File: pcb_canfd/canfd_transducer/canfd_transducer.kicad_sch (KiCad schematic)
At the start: 7 parts, among them J1 Conn_01x13_Female, J2 Conn_01x03_Female, U1 MCP2517FD-xSL

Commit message: finished first version of board, needs revision
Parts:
- added H1, H2, H3, H4: MountingHole, MountingHole:MountingHole_3.2mm_M3_DIN965_Pad_TopOnly, symbol Mechanical:MountingHole
- J1: footprint Connector_PinHeader_2.54mm:PinHeader_1x13_P2.54mm_Vertical -> Connector_PinSocket_2.54mm:PinSocket_1x13_P2.54mm_Vertical
- renumbered 11 to U2
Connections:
- net +3.3V: now also J1.3 (Pin_3); no longer J1.2 (Pin_2)
- net CANH: now also J2.1 (Pin_1); no longer J2.2 (Pin_2)
- net CANL: now also J2.2 (Pin_2); no longer J2.3 (Pin_3)
- net CLKO: now also J1.13 (Pin_13); no longer J1.8 (Pin_8)
- net GND: now also J1.2 (Pin_2), J2.3 (Pin_3); no longer J1.3 (Pin_3)
- net OSC2: now also J1.11 (Pin_11); no longer J1.9 (Pin_9)
- net SDI: now also J1.6 (Pin_6); no longer J1.4 (Pin_4)
- net nCS: now also J1.4 (Pin_4); no longer J1.6 (Pin_6)
- net ~{INT0}: now also J1.8 (Pin_8); no longer J1.12 (Pin_12)
- net ~{INT1}: now also J1.9 (Pin_9); no longer J1.11 (Pin_11)
- net ~{INT}: now also J1.12 (Pin_12); no longer J1.13 (Pin_13)

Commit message: small changes
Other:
- company: (none) -> Group 3 - ME410, EPFL
- title: (none) -> SPI to can FD transducer
- moved on the sheet: H1, H2, H3, H4
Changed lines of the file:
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@@
 (kicad_sch (version 20211123) (generator eeschema)
   (paper "A4")
+  (title_block
+    (title "SPI to can FD transducer")
+    (date "2023-10-23")
+    (company "Group 3 - ME410, EPFL")
+  )
   (junction (at 81.28 67.31) (diameter 0) (color 0 0 0 0)
   )
@@
     (pin "2")
   )
-  (symbol (lib_id "Mechanical:MountingHole") (at 252.73 124.46 0) (unit 1)
-    (in_bom yes) (on_board yes) (fields_autoplaced)
-    (property "Reference" "H3" (id 0) (at 255.27 123.1899 0)
-      (effects (font (size 1.27 1.27)) (justify left))
-    )
-    (property "Value" "MountingHole" (id 1) (at 255.27 125.7299 0)
-      (effects (font (size 1.27 1.27)) (justify left))
-    )
-    (property "Footprint" "MountingHole:MountingHole_3.2mm_M3_DIN965_Pad_TopOnly" (id 2) (at 252.73 124.46 0)
-      (effects (font (size 1.27 1.27)) hide)
-    )
-    (property "Datasheet" "~" (id 3) (at 252.73 124.46 0)
+  (symbol (lib_id "Mechanical:MountingHole") (at 234.95 57.15 0) (unit 1)
+    (in_bom yes) (on_board yes) (fields_autoplaced)
+    (property "Reference" "H3" (id 0) (at 237.49 55.8799 0)
+      (effects (font (size 1.27 1.27)) (justify left))
+    )
+    (property "Value" "MountingHole" (id 1) (at 237.49 58.4199 0)
+      (effects (font (size 1.27 1.27)) (justify left))
+    )
+    (property "Footprint" "MountingHole:MountingHole_3.2mm_M3_DIN965_Pad_TopOnly" (id 2) (at 234.95 57.15 0)
+      (effects (font (size 1.27 1.27)) hide)
+    )
+    (property "Datasheet" "~" (id 3) (at 234.95 57.15 0)
       (effects (font (size 1.27 1.27)) hide)
     )
@@
     (pin "8")
   )
-  (symbol (lib_id "Mechanical:MountingHole") (at 252.73 130.81 0) (unit 1)
-    (in_bom yes) (on_board yes) (fields_autoplaced)
-    (property "Reference" "H4" (id 0) (at 255.27 129.5399 0)
-      (effects (font (size 1.27 1.27)) (justify left))
-    )
-    (property "Value" "MountingHole" (id 1) (at 255.27 132.0799 0)
-      (effects (font (size 1.27 1.27)) (justify left))
-    )
-    (property "Footprint" "MountingHole:MountingHole_3.2mm_M3_DIN965_Pad_TopOnly" (id 2) (at 252.73 130.81 0)
-      (effects (font (size 1.27 1.27)) hide)
-    )
-    (property "Datasheet" "~" (id 3) (at 252.73 130.81 0)
+  (symbol (lib_id "Mechanical:MountingHole") (at 234.95 63.5 0) (unit 1)
+    (in_bom yes) (on_board yes) (fields_autoplaced)
+    (property "Reference" "H4" (id 0) (at 237.49 62.2299 0)
+      (effects (font (size 1.27 1.27)) (justify left))
+    )
+    (property "Value" "MountingHole" (id 1) (at 237.49 64.7699 0)
+      (effects (font (size 1.27 1.27)) (justify left))
+    )
+    (property "Footprint" "MountingHole:MountingHole_3.2mm_M3_DIN965_Pad_TopOnly" (id 2) (at 234.95 63.5 0)
+      (effects (font (size 1.27 1.27)) hide)
+    )
+    (property "Datasheet" "~" (id 3) (at 234.95 63.5 0)
       (effects (font (size 1.27 1.27)) hide)
     )
@@
     (pin "1")
   )
-  (symbol (lib_id "Mechanical:MountingHole") (at 252.73 118.11 0) (unit 1)
-    (in_bom yes) (on_board yes) (fields_autoplaced)
-    (property "Reference" "H2" (id 0) (at 255.27 116.8399 0)
-      (effects (font (size 1.27 1.27)) (justify left))
-    )
-    (property "Value" "MountingHole" (id 1) (at 255.27 119.3799 0)
-      (effects (font (size 1.27 1.27)) (justify left))
-    )
-    (property "Footprint" "MountingHole:MountingHole_3.2mm_M3_DIN965_Pad_TopOnly" (id 2) (at 252.73 118.11 0)
-      (effects (font (size 1.27 1.27)) hide)
-    )
-    (property "Datasheet" "~" (id 3) (at 252.73 118.11 0)
+  (symbol (lib_id "Mechanical:MountingHole") (at 234.95 50.8 0) (unit 1)
+    (in_bom yes) (on_board yes) (fields_autoplaced)
+    (property "Reference" "H2" (id 0) (at 237.49 49.5299 0)
+      (effects (font (size 1.27 1.27)) (justify left))
+    )
+    (property "Value" "MountingHole" (id 1) (at 237.49 52.0699 0)
+      (effects (font (size 1.27 1.27)) (justify left))
+    )
+    (property "Footprint" "MountingHole:MountingHole_3.2mm_M3_DIN965_Pad_TopOnly" (id 2) (at 234.95 50.8 0)
+      (effects (font (size 1.27 1.27)) hide)
+    )
+    (property "Datasheet" "~" (id 3) (at 234.95 50.8 0)
       (effects (font (size 1.27 1.27)) hide)
     )
@@
     (pin "1")
   )
-  (symbol (lib_id "Mechanical:MountingHole") (at 252.73 111.76 0) (unit 1)
-    (in_bom yes) (on_board yes) (fields_autoplaced)
-    (property "Reference" "H1" (id 0) (at 255.27 110.4899 0)
-      (effects (font (size 1.27 1.27)) (justify left))
-    )
-    (property "Value" "MountingHole" (id 1) (at 255.27 113.0299 0)
-      (effects (font (size 1.27 1.27)) (justify left))
-    )
-    (property "Footprint" "MountingHole:MountingHole_3.2mm_M3_DIN965_Pad_TopOnly" (id 2) (at 252.73 111.76 0)
-      (effects (font (size 1.27 1.27)) hide)
-    )
-    (property "Datasheet" "~" (id 3) (at 252.73 111.76 0)
-      (effects (font (size 1.27 1.27)) hide)
-    )
+  (symbol (lib_id "Mechanical:MountingHole") (at 234.95 44.45 0) (unit 1)
+    (in_bom yes) (on_board yes) (fields_autoplaced)
+    (property "Reference" "H1" (id 0) (at 237.49 43.1799 0)
+      (effects (font (size 1.27 1.27)) (justify left))
+    )
+    (property "Value" "MountingHole" (id 1) (at 237.49 45.7199 0)
+      (effects (font (size 1.27 1.27)) (justify left))
+    )
+    (property "Footprint" "MountingHole:MountingHole_3.2mm_M3_DIN965_Pad_TopOnly" (id 2) (at 234.95 44.45 0)
+      (effects (font (size 1.27 1.27)) hide)
+    )
+    (property "Datasheet" "~" (id 3) (at 234.95 44.45 0)
+      (effects (font (size 1.27 1.27)) hide)
+    )

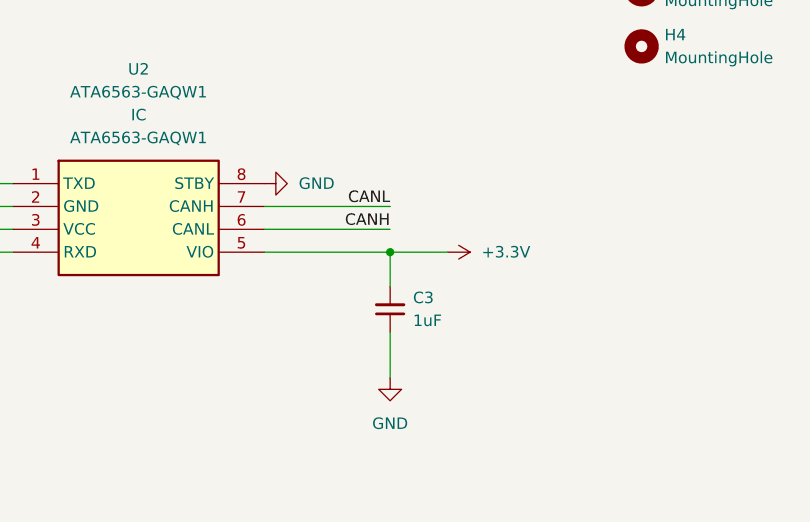
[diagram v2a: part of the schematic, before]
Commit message: added resistor for can bus
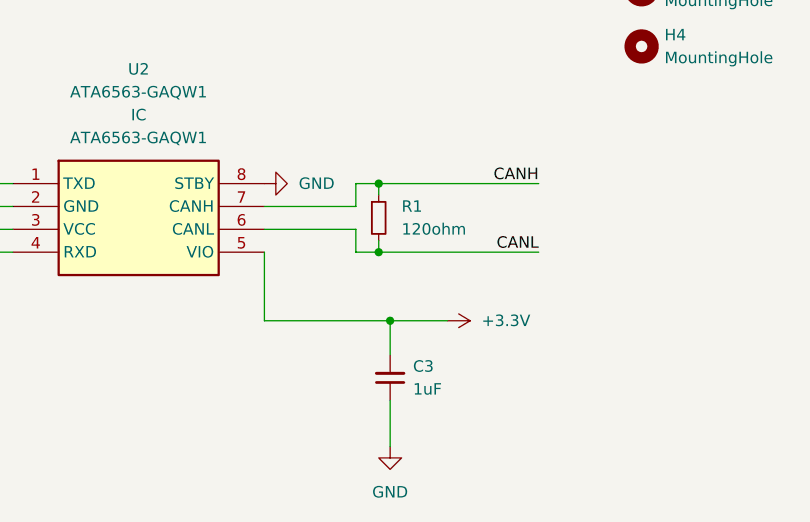
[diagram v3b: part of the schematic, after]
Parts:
- added R1: 120ohm, Resistor_SMD:R_0805_2012Metric, symbol Device:R_Small
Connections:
- net CANH: now also U2.7 (CANH), R1.1; no longer U2.6 (CANL)
- net CANL: now also U2.6 (CANL), R1.2; no longer U2.7 (CANH)
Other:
- moved on the sheet: C3
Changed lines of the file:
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@@
     (company "Group 3 - ME410, EPFL")
   )
+  (junction (at 205.74 78.74) (diameter 0) (color 0 0 0 0)
+  )
+  (junction (at 207.01 93.98) (diameter 0) (color 0 0 0 0)
+  )
+  (junction (at 205.74 86.36) (diameter 0) (color 0 0 0 0)
+  )
   (junction (at 81.28 67.31) (diameter 0) (color 0 0 0 0)
   )
   (junction (at 144.78 83.82) (diameter 0) (color 0 0 0 0)
   )
-  (junction (at 207.01 86.36) (diameter 0) (color 0 0 0 0)
-  )
-  (wire (pts (xy 207.01 100.33) (xy 207.01 95.25))
+  (wire (pts (xy 207.01 107.95) (xy 207.01 102.87))
+    (stroke (width 0) (type default) (color 0 0 0 0))
+  )
+  (wire (pts (xy 205.74 78.74) (xy 223.52 78.74))
     (stroke (width 0) (type default) (color 0 0 0 0))
   )
@@
     (stroke (width 0) (type default) (color 0 0 0 0))
   )
+  (wire (pts (xy 203.2 83.82) (xy 203.2 86.36))
+    (stroke (width 0) (type default) (color 0 0 0 0))
+  )
   (wire (pts (xy 142.24 83.82) (xy 144.78 83.82))
     (stroke (width 0) (type default) (color 0 0 0 0))
@@
     (stroke (width 0) (type default) (color 0 0 0 0))
   )
+  (wire (pts (xy 205.74 86.36) (xy 223.52 86.36))
+    (stroke (width 0) (type default) (color 0 0 0 0))
+  )
+  (wire (pts (xy 203.2 86.36) (xy 205.74 86.36))
+    (stroke (width 0) (type default) (color 0 0 0 0))
+  )
   (wire (pts (xy 179.07 35.56) (xy 165.1 35.56))
     (stroke (width 0) (type default) (color 0 0 0 0))
@@
     (stroke (width 0) (type default) (color 0 0 0 0))
   )
-  (wire (pts (xy 193.04 86.36) (xy 207.01 86.36))
-    (stroke (width 0) (type default) (color 0 0 0 0))
-  )
-  (wire (pts (xy 207.01 86.36) (xy 207.01 90.17))
+  (wire (pts (xy 207.01 93.98) (xy 207.01 97.79))
     (stroke (width 0) (type default) (color 0 0 0 0))
   )
@@
     (stroke (width 0) (type default) (color 0 0 0 0))
   )
+  (wire (pts (xy 193.04 93.98) (xy 207.01 93.98))
+    (stroke (width 0) (type default) (color 0 0 0 0))
+  )
   (wire (pts (xy 66.04 67.31) (xy 71.12 67.31))
     (stroke (width 0) (type default) (color 0 0 0 0))
   )
+  (wire (pts (xy 205.74 86.36) (xy 205.74 85.09))
+    (stroke (width 0) (type default) (color 0 0 0 0))
+  )
   (wire (pts (xy 144.78 97.79) (xy 144.78 92.71))
     (stroke (width 0) (type default) (color 0 0 0 0))
   )
-  (wire (pts (xy 193.04 81.28) (xy 207.01 81.28))
+  (wire (pts (xy 203.2 81.28) (xy 203.2 78.74))
     (stroke (width 0) (type default) (color 0 0 0 0))
   )
@@
     (stroke (width 0) (type default) (color 0 0 0 0))
   )
+  (wire (pts (xy 205.74 78.74) (xy 205.74 80.01))
+    (stroke (width 0) (type default) (color 0 0 0 0))
+  )
   (wire (pts (xy 179.07 38.1) (xy 165.1 38.1))
     (stroke (width 0) (type default) (color 0 0 0 0))
   )
+  (wire (pts (xy 203.2 78.74) (xy 205.74 78.74))
+    (stroke (width 0) (type default) (color 0 0 0 0))
+  )
   (wire (pts (xy 160.02 81.28) (xy 165.1 81.28))
     (stroke (width 0) (type default) (color 0 0 0 0))
@@
     (stroke (width 0) (type default) (color 0 0 0 0))
   )
+  (wire (pts (xy 193.04 83.82) (xy 203.2 83.82))
+    (stroke (width 0) (type default) (color 0 0 0 0))
+  )
+  (wire (pts (xy 193.04 81.28) (xy 203.2 81.28))
+    (stroke (width 0) (type default) (color 0 0 0 0))
+  )
   (wire (pts (xy 96.52 78.74) (xy 109.22 78.74))
     (stroke (width 0) (type default) (color 0 0 0 0))
@@
     (stroke (width 0) (type default) (color 0 0 0 0))
   )
-  (wire (pts (xy 193.04 83.82) (xy 207.01 83.82))
-    (stroke (width 0) (type default) (color 0 0 0 0))
-  )
   (wire (pts (xy 110.49 29.21) (xy 123.19 29.21))
     (stroke (width 0) (type default) (color 0 0 0 0))
   )
-  (wire (pts (xy 207.01 86.36) (xy 213.36 86.36))
+  (wire (pts (xy 207.01 93.98) (xy 213.36 93.98))
+    (stroke (width 0) (type default) (color 0 0 0 0))
+  )
+  (wire (pts (xy 193.04 86.36) (xy 193.04 93.98))
     (stroke (width 0) (type default) (color 0 0 0 0))
   )
@@
     (effects (font (size 1.27 1.27)) (justify left bottom))
   )
-  (label "CANH" (at 207.01 83.82 180)
-    (effects (font (size 1.27 1.27)) (justify right bottom))
-  )
   (label "CLKO" (at 109.22 83.82 180)
     (effects (font (size 1.27 1.27)) (justify right bottom))
@@
     (effects (font (size 1.27 1.27)) (justify left bottom))
   )
+  (label "CANL" (at 223.52 86.36 180)
+    (effects (font (size 1.27 1.27)) (justify right bottom))
+  )
   (label "CAN_RX" (at 153.67 86.36 0)
     (effects (font (size 1.27 1.27)) (justify left bottom))
@@
   (label "OSC2" (at 52.07 91.44 0)
     (effects (font (size 1.27 1.27)) (justify left bottom))
+  )
+  (label "CANH" (at 223.52 78.74 180)
+    (effects (font (size 1.27 1.27)) (justify right bottom))
   )
   (label "SCK" (at 52.07 86.36 0)
@@
     (effects (font (size 1.27 1.27)) (justify left bottom))
   )
-  (label "CANL" (at 207.01 81.28 180)
-    (effects (font (size 1.27 1.27)) (justify right bottom))
-  )
   (label "CANH" (at 165.1 33.02 0)
     (effects (font (size 1.27 1.27)) (justify left bottom))
@@
   (symbol (lib_id "power:GND") (at 165.1 38.1 270) (unit 1)
     (in_bom yes) (on_board yes)
-    (property "Reference" "#PWR?" (id 0) (at 158.75 38.1 0)
+    (property "Reference" "#PWR0113" (id 0) (at 158.75 38.1 0)
       (effects (font (size 1.27 1.27)) hide)
     )
@@
     (pin "1")
   )
-  (symbol (lib_id "Device:C_Small") (at 207.01 92.71 180) (unit 1)
-    (in_bom yes) (on_board yes) (fields_autoplaced)
-    (property "Reference" "C3" (id 0) (at 209.55 91.4335 0)
+  (symbol (lib_id "Device:C_Small") (at 207.01 100.33 180) (unit 1)
+    (in_bom yes) (on_board yes) (fields_autoplaced)
+    (property "Reference" "C3" (id 0) (at 209.55 99.0535 0)
       (effects (font (size 1.27 1.27)) (justify right))
     )
-    (property "Value" "1uF" (id 1) (at 209.55 93.9735 0)
+    (property "Value" "1uF" (id 1) (at 209.55 101.5935 0)
       (effects (font (size 1.27 1.27)) (justify right))
     )
-    (property "Footprint" "Capacitor_SMD:C_0603_1608Metric" (id 2) (at 207.01 92.71 0)
-      (effects (font (size 1.27 1.27)) hide)
-    )
-    (property "Datasheet" "~" (id 3) (at 207.01 92.71 0)
+    (property "Footprint" "Capacitor_SMD:C_0603_1608Metric" (id 2) (at 207.01 100.33 0)
+      (effects (font (size 1.27 1.27)) hide)
+    )
+    (property "Datasheet" "~" (id 3) (at 207.01 100.33 0)
       (effects (font (size 1.27 1.27)) hide)
     )
@@
     (pin "7")
     (pin "8")
+  )
+  (symbol (lib_id "Device:R_Small") (at 205.74 82.55 0) (unit 1)
+    (in_bom yes) (on_board yes)
+    (property "Reference" "R1" (id 0) (at 208.28 81.2799 0)
+      (effects (font (size 1.27 1.27)) (justify left))
+    )
+    (property "Value" "120ohm" (id 1) (at 208.28 83.82 0)
+      (effects (font (size 1.27 1.27)) (justify left))
+    )
+    (property "Footprint" "Resistor_SMD:R_0805_2012Metric" (id 2) (at 205.74 82.55 0)
+      (effects (font (size 1.27 1.27)) hide)
+    )
+    (property "Datasheet" "~" (id 3) (at 205.74 82.55 0)
+      (effects (font (size 1.27 1.27)) hide)
+    )
+    (pin "1")
+    (pin "2")
   )
   (symbol (lib_id "Mechanical:MountingHole") (at 234.95 63.5 0) (unit 1)
@@
     (pin "1")
   )
-  (symbol (lib_id "power:GND") (at 207.01 100.33 0) (unit 1)
-    (in_bom yes) (on_board yes) (fields_autoplaced)
-    (property "Reference" "#PWR0107" (id 0) (at 207.01 106.68 0)
-      (effects (font (size 1.27 1.27)) hide)
-    )
-    (property "Value" "GND" (id 1) (at 207.01 105.41 0))
-    (property "Footprint" "" (id 2) (at 207.01 100.33 0)
-      (effects (font (size 1.27 1.27)) hide)
-    )
-    (property "Datasheet" "" (id 3) (at 207.01 100.33 0)
+  (symbol (lib_id "power:GND") (at 207.01 107.95 0) (unit 1)
+    (in_bom yes) (on_board yes) (fields_autoplaced)
+    (property "Reference" "#PWR0107" (id 0) (at 207.01 114.3 0)
+      (effects (font (size 1.27 1.27)) hide)
+    )
+    (property "Value" "GND" (id 1) (at 207.01 113.03 0))
+    (property "Footprint" "" (id 2) (at 207.01 107.95 0)
+      (effects (font (size 1.27 1.27)) hide)
+    )
+    (property "Datasheet" "" (id 3) (at 207.01 107.95 0)
       (effects (font (size 1.27 1.27)) hide)
     )
@@
     (pin "1")
   )
-  (symbol (lib_id "power:+3.3V") (at 213.36 86.36 270) (unit 1)
-    (in_bom yes) (on_board yes) (fields_autoplaced)
-    (property "Reference" "#PWR0106" (id 0) (at 209.55 86.36 0)
-      (effects (font (size 1.27 1.27)) hide)
-    )
-    (property "Value" "+3.3V" (id 1) (at 217.17 86.3599 90)
-      (effects (font (size 1.27 1.27)) (justify left))
-    )
-    (property "Footprint" "" (id 2) (at 213.36 86.36 0)
-      (effects (font (size 1.27 1.27)) hide)
-    )
-    (property "Datasheet" "" (id 3) (at 213.36 86.36 0)
+  (symbol (lib_id "power:+3.3V") (at 213.36 93.98 270) (unit 1)
+    (in_bom yes) (on_board yes) (fields_autoplaced)
+    (property "Reference" "#PWR0106" (id 0) (at 209.55 93.98 0)
+      (effects (font (size 1.27 1.27)) hide)
+    )
+    (property "Value" "+3.3V" (id 1) (at 217.17 93.9799 90)
+      (effects (font (size 1.27 1.27)) (justify left))
+    )
+    (property "Footprint" "" (id 2) (at 213.36 93.98 0)
+      (effects (font (size 1.27 1.27)) hide)
+    )
+    (property "Datasheet" "" (id 3) (at 213.36 93.98 0)
       (effects (font (size 1.27 1.27)) hide)
     )
@@
     )
     (path "/05f14cb7-6472-467c-be1a-efba32b4b8fc"
-      (reference "#PWR?") (unit 1) (value "GND") (footprint "")
+      (reference "#PWR0113") (unit 1) (value "GND") (footprint "")
     )
     (path "/a915fb01-56c1-4170-b657-1f0184c2dccd"
@@
       (reference "J2") (unit 1) (value "Conn_01x03_Female") (footprint "Connector_JST:JST_PH_B3B-PH-K_1x03_P2.00mm_Vertical")
     )
+    (path "/36226126-9291-47cc-81b9-966147919741"
+      (reference "R1") (unit 1) (value "120ohm") (footprint "Resistor_SMD:R_0805_2012Metric")
+    )
     (path "/4a2c41ae-4c1b-40fa-ba2f-1bdb8c44041e"
